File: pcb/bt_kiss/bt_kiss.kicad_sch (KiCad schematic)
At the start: 18 parts, among them J1 HC-05, J2 to_radio, J3 5v PWR, J4 Bat_Plus, J5 Bat_GND, J6 Bat input, J7 Key, Q1 PN2222A, SW1 SW_Push

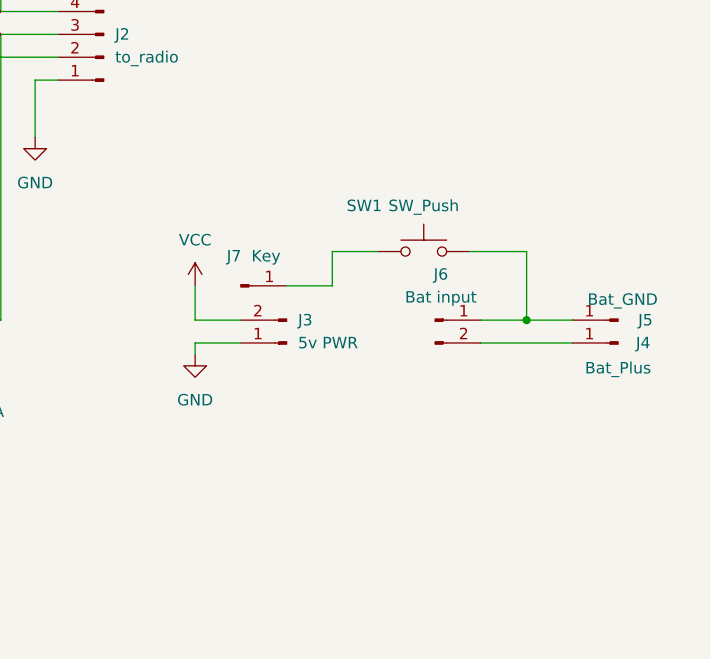
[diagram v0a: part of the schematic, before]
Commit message: added 18650 battery holder for the BT KISS TNC PCB
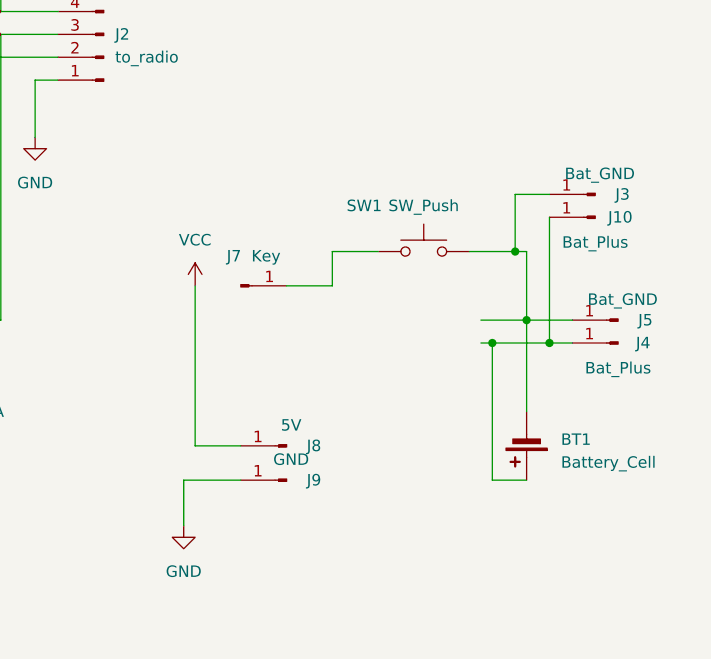
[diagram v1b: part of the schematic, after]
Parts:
- removed J3: 5v PWR, Connector_PinSocket_2.54mm:PinSocket_1x02_P2.54mm_Vertical, symbol Connector:Conn_01x02_Pin
- removed J6: Bat input, Connector_PinHeader_2.54mm:PinHeader_1x02_P2.54mm_Vertical, symbol Connector:Conn_01x02_Pin
- added BT1: Battery_Cell, Battery:BatteryHolder_Keystone_1042_1x18650, symbol Device:Battery_Cell
- added J10: Bat_Plus, Connector_PinHeader_2.54mm:PinHeader_1x01_P2.54mm_Vertical, symbol Connector:Conn_01x01_Pin
- added J3: Bat_GND, Connector_PinHeader_2.54mm:PinHeader_1x01_P2.54mm_Vertical, symbol Connector:Conn_01x01_Pin
- added J8: 5V, Connector_PinHeader_2.54mm:PinHeader_1x01_P2.54mm_Vertical, symbol Connector:Conn_01x01_Pin
- added J9: GND, Connector_PinHeader_2.54mm:PinHeader_1x01_P2.54mm_Vertical, symbol Connector:Conn_01x01_Pin
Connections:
- net GND: now also J9.1 (Pin_1)
- net VCC: now also J8.1 (Pin_1)
- net at J5.1 (Pin_1), SW1.2: now also BT1.2 (-), J3.1 (Pin_1)
- net at J4.1 (Pin_1): now also BT1.1 (+), J10.1 (Pin_1)

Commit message: added KISS TNC read me: 2025-04-07 18:54:28
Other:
- note added: "1.0"
- note added: "APRS Bluetooth KISS TNC with a Liion 18650"
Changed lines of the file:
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@@
+		)
+	)
+	(text "APRS Bluetooth KISS TNC with a Liion 18650 "
+		(exclude_from_sim no)
+		(at 121.92 127.762 0)
+		(effects
+			(font
+				(size 1.27 1.27)
+			)
+		)
+	)
+	(text "1.0"
+		(exclude_from_sim no)
+		(at 182.88 131.318 0)
+		(effects
+			(font
+				(size 1.27 1.27)
+			)
 		)
 	)
